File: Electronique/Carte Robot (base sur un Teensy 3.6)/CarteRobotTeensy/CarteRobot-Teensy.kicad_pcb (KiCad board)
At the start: 2 copper layers, 1 part, among them J1 Teensy-3.6

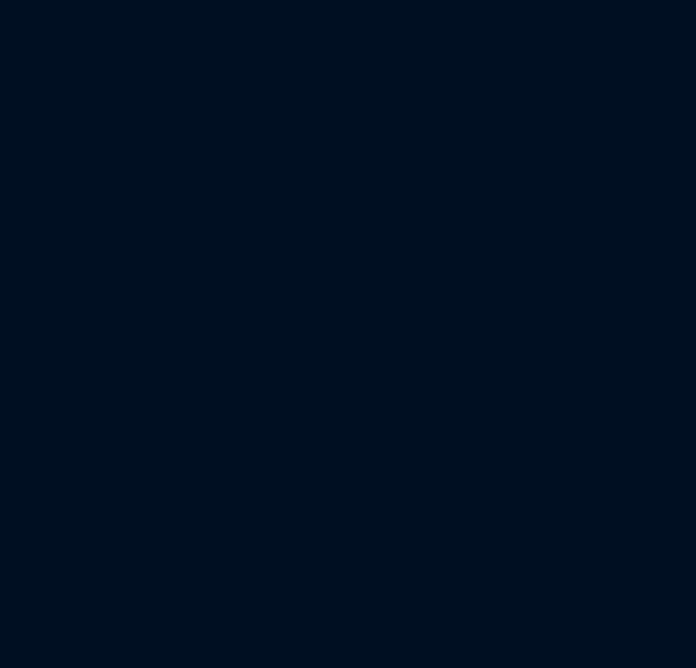
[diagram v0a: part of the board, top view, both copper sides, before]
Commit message: maj schema de la carte robot
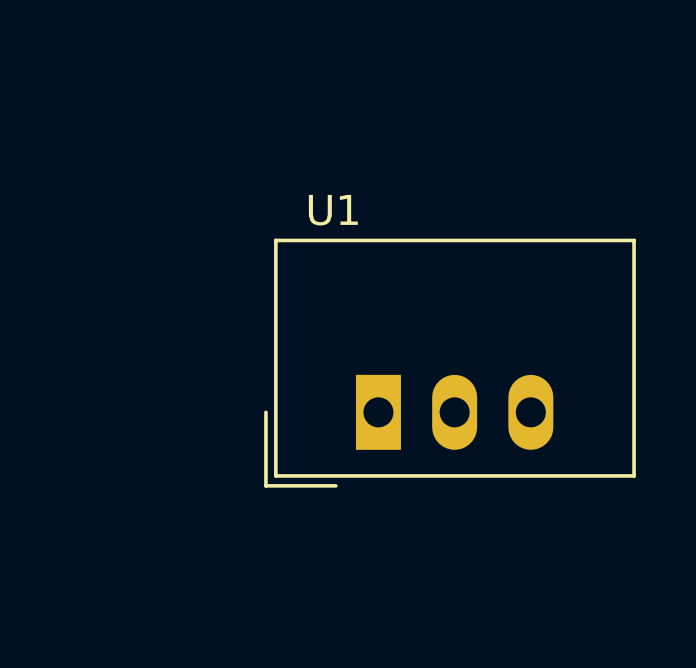
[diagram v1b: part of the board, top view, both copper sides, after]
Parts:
- added U1: TSR_1-2450, Converter_DCDC:Converter_DCDC_TRACO_TSR-1_THT, F.Cu at (397.5, 236.2)
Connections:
- J1 pad 1: Net-(J1-Pad1) -> GND
- J1 pad 34: Net-(J1-Pad34) -> GND
- J1 pad 48: Net-(J1-Pad48) -> +5V

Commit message: ajout driver schema de la carte
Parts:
- added A1: Pololu_Breakout_DRV8825, Module:Pololu_Breakout-16_15.2x20.3mm, F.Cu at (111.0, 102.0)
- added A2: Pololu_Breakout_DRV8825, Module:Pololu_Breakout-16_15.2x20.3mm, F.Cu at (134.7, 135.8)
- added D2: 1N4001, Diode_THT:D_DO-41_SOD81_P10.16mm_Horizontal, F.Cu at (130.0, 68.0)
- added J1: Conn_Bat2, Mes_empreintes:SL_3.50-02-180G_Weidmuller, F.Cu at (127.5, 58.0)
- added J10: Conn_01x03, Connector_PinHeader_2.54mm:PinHeader_1x03_P2.54mm_Vertical, F.Cu at (109.0, 123.0)
- added J11: Conn_AX12, Connector_Molex:Molex_SPOX_5267-03A_1x03_P2.50mm_Vertical, F.Cu at (218.0, 94.0)
- added J2: Conn_Bat1, Mes_empreintes:SL_3.50-02-180G_Weidmuller, F.Cu at (140.5, 58.0)
- added J3: Conn_OnOff, Connector_PinHeader_2.54mm:PinHeader_1x02_P2.54mm_Vertical, F.Cu at (117.0, 57.0)
- added J4: Conn_Aru, Connector_PinHeader_2.54mm:PinHeader_1x02_P2.54mm_Vertical, F.Cu at (104.0, 57.0)
- added J8: Conn_01x03, Connector_PinHeader_2.54mm:PinHeader_1x03_P2.54mm_Vertical, F.Cu at (92.0, 123.0)
- added J9: Conn_01x03, Connector_PinHeader_2.54mm:PinHeader_1x03_P2.54mm_Vertical, F.Cu at (101.0, 123.0)
- added U2: TSR_1-2465, Converter_DCDC:Converter_DCDC_TRACO_TSR-1_THT, F.Cu at (190.8, 38.3)
- added U3: TSR_1-2490, Converter_DCDC:Converter_DCDC_TRACO_TSR-1_THT, F.Cu at (190.8, 53.0)
- moved U1 334.2 mm to (107.0, 71.0)
- moved J5 322.4 mm to (61.9, 74.5)
- renumbered J1 to J5
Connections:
- net Net-(J1-Pad45) renamed /Vbat
- J5 pad 15: Net-(J1-Pad15) -> +3V3
- J5 pad 27: Net-(J1-Pad27) -> /STEP_D
- J5 pad 28: Net-(J1-Pad28) -> /STEP_G
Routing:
- net /M2: track 0.00 -> 16.8 mm
- net /M0: track 0.00 -> 14.4 mm
- net /M1: track 0.00 -> 13.4 mm
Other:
- board outline added: 100 x 100 mm

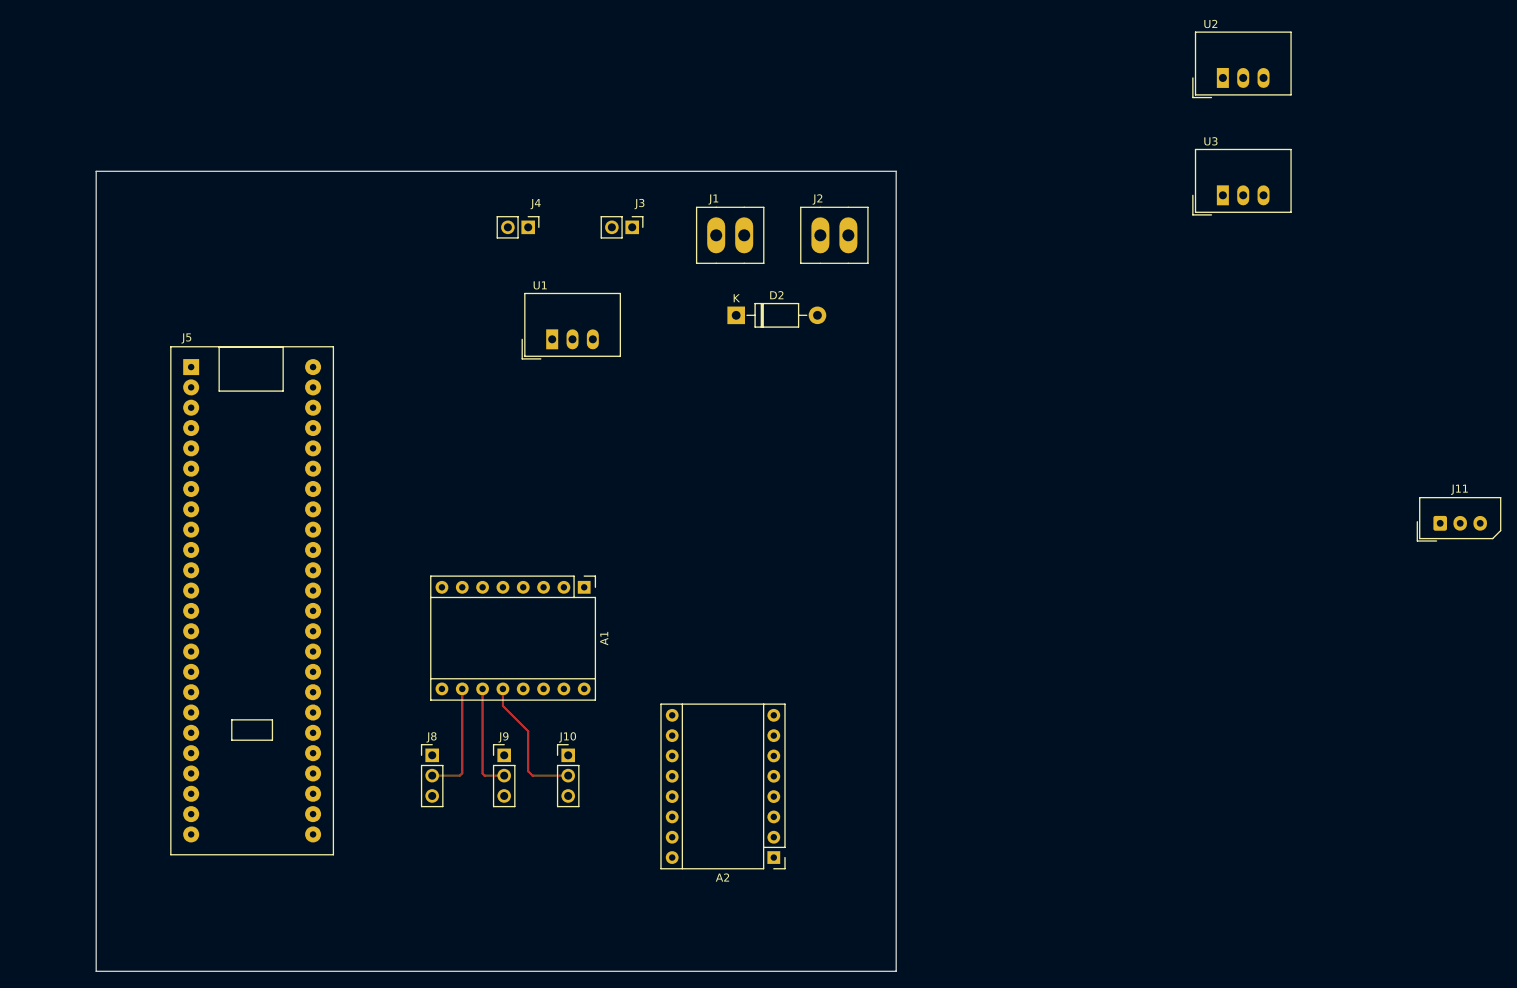
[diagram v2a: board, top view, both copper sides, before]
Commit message: ajouts des connecteurs pour l'uart
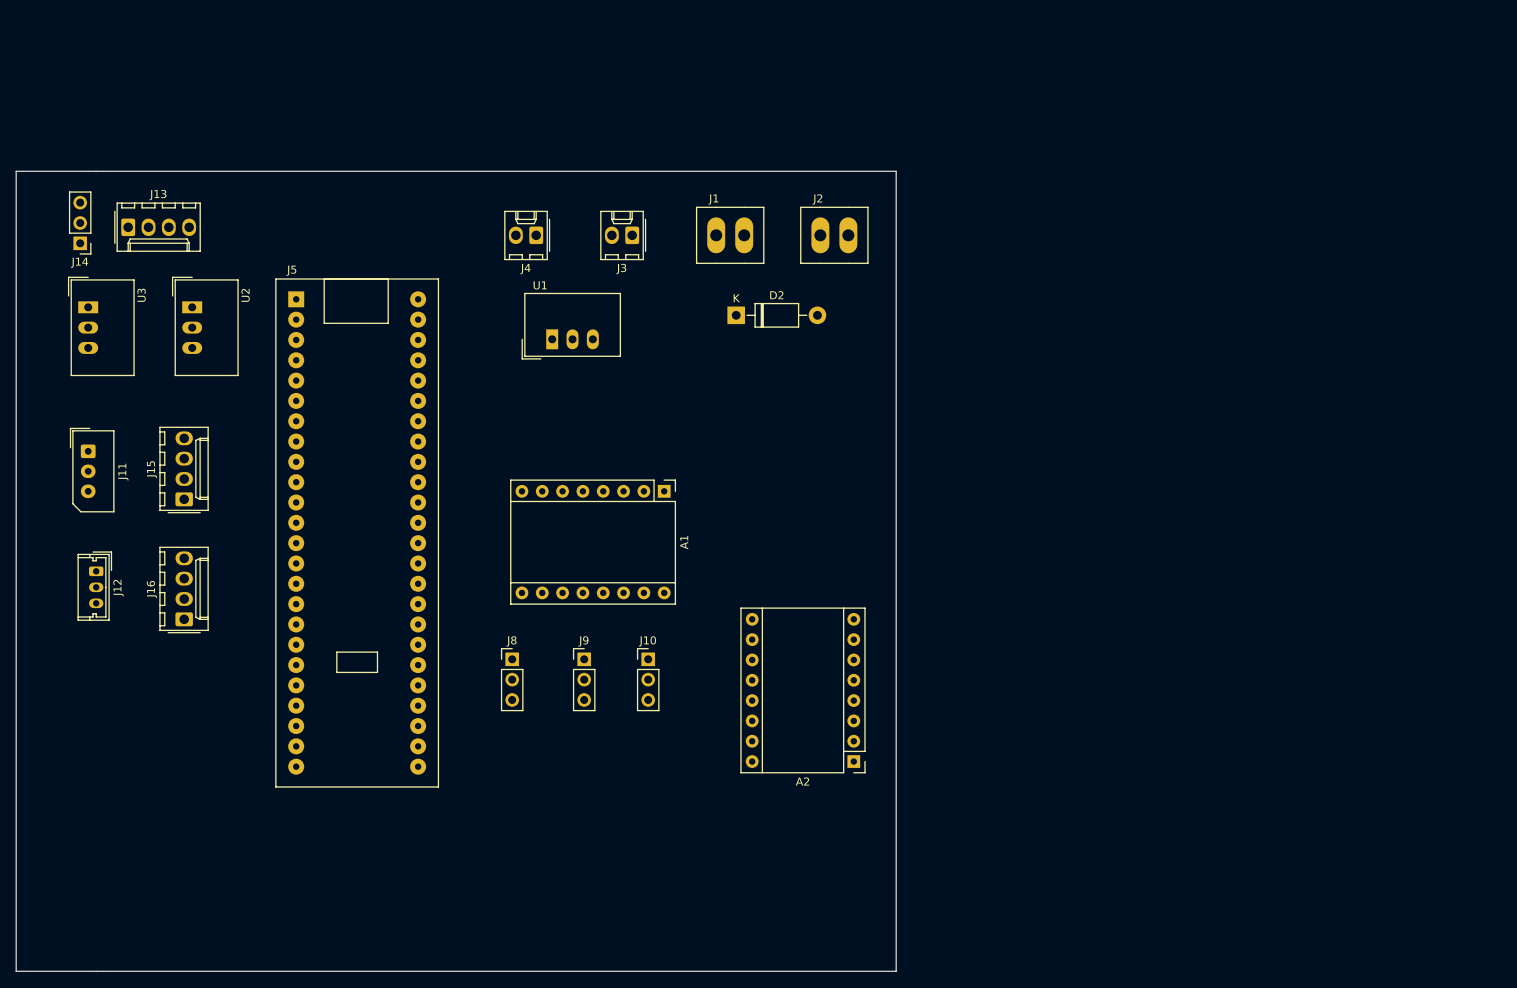
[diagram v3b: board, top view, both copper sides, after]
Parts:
- added J12: Conn_XL320, Connector_Molex:Molex_Micro-Latch_53253-0370_1x03_P2.00mm_Vertical, F.Cu at (50.0, 100.0)
- added J13: Conn_01x04, Connector_Molex:Molex_KK-254_AE-6410-04A_1x04_P2.54mm_Vertical, F.Cu at (54.0, 57.0)
- added J14: Conn_01x03, Connector_PinHeader_2.54mm:PinHeader_1x03_P2.54mm_Vertical, F.Cu at (48.0, 59.0)
- added J15: Conn_01x04, Connector_Molex:Molex_KK-254_AE-6410-04A_1x04_P2.54mm_Vertical, F.Cu at (61.0, 91.0)
- added J16: Conn_01x04, Connector_Molex:Molex_KK-254_AE-6410-04A_1x04_P2.54mm_Vertical, F.Cu at (61.0, 106.0)
- J3, J4: footprint Connector_PinHeader_2.54mm:PinHeader_1x02_P2.54mm_Vertical -> Connector_Molex:Molex_KK-254_AE-6410-02A_1x02_P2.54mm_Vertical
- moved J11 169.2 mm to (49.0, 85.0), turned to 270 degrees
- moved U3 142.5 mm to (49.0, 67.0), turned to 270 degrees
- moved U2 132.0 mm to (62.0, 67.0), turned to 270 degrees
- moved J5 15.6 mm to (75.0, 66.0)
- moved A1 15.6 mm to (121.0, 90.0)
- moved A2 15.6 mm to (144.7, 123.8)
- moved J10 15.6 mm to (119.0, 111.0)
- moved J8 15.6 mm to (102.0, 111.0)
- moved J9 15.6 mm to (111.0, 111.0)
- moved J4 1.41 mm to (105.0, 58.0), turned to 180 degrees
- moved J3 1.00 mm to (117.0, 58.0), turned to 180 degrees
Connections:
- net Net-(J5-Pad2) renamed /RX1
- net Net-(J5-Pad3) renamed /TX1
- J11 pad 1: Net-(J11-Pad1) -> GND
- J11 pad 2: Net-(J11-Pad2) -> +9V
- J11 pad 3: Net-(J11-Pad3) -> /TX3
- J5 pad 10: Net-(J5-Pad10) -> /TX2
- J5 pad 7: Net-(J5-Pad7) -> /RX3
- J5 pad 8: Net-(J5-Pad8) -> /TX3
- J5 pad 9: Net-(J5-Pad9) -> /RX2
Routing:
- net /M2: track 16.8 -> 0.00 mm
- net /M0: track 14.4 -> 0.00 mm
- net /M1: track 13.4 -> 0.00 mm
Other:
- board size 100 x 100 mm -> 110 x 100 mm

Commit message: ajouts connecteurs, leds
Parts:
- added C1: 100u, Capacitor_THT:CP_Radial_D6.3mm_P2.50mm, F.Cu at (103.0, 92.0)
- added C2: 100u, Capacitor_THT:CP_Radial_D6.3mm_P2.50mm, F.Cu at (132.0, 110.0)
- added D1: LED, LED_THT:LED_D5.0mm_Clear, F.Cu at (122.0, 68.0)
- added J17: Conn_01x04, Connector_Molex:Molex_KK-254_AE-6410-04A_1x04_P2.54mm_Vertical, F.Cu at (70.5, 133.0)
- added J18: Conn_01x04, Connector_Molex:Molex_KK-254_AE-6410-04A_1x04_P2.54mm_Vertical, F.Cu at (86.0, 133.0)
- added J19: Conn_01x03, Connector_Molex:Molex_KK-254_AE-6410-03A_1x03_P2.54mm_Vertical, F.Cu at (144.0, 71.0)
- added J20: Conn_01x04, Connector_Molex:Molex_KK-254_AE-6410-04A_1x04_P2.54mm_Vertical, F.Cu at (144.0, 81.5)
- added J21: Conn_01x04, Connector_Molex:Molex_KK-254_AE-6410-04A_1x04_P2.54mm_Vertical, F.Cu at (135.0, 81.5)
- added J6: Conn_01x04, Connector_Molex:Molex_KK-254_AE-6410-04A_1x04_P2.54mm_Vertical, F.Cu at (145.0, 96.5)
- added J7: Conn_01x04, Connector_Molex:Molex_KK-254_AE-6410-04A_1x04_P2.54mm_Vertical, F.Cu at (145.0, 117.0)
- added R1: 100k, Resistor_SMD:R_0805_2012Metric_Pad1.20x1.40mm_HandSolder, F.Cu at (116.0, 66.0)
- moved J10 14.0 mm to (119.0, 125.0), turned to 180 degrees
- moved J8 14.0 mm to (102.0, 125.0), turned to 180 degrees
- moved J9 14.0 mm to (111.0, 125.0), turned to 180 degrees
- moved A2 11.7 mm to (139.0, 134.0)
- moved A1 9.00 mm to (121.0, 99.0)
- moved U1 6.32 mm to (109.0, 65.0), turned to 180 degrees
- moved D2 3.61 mm to (128.0, 65.0)
- moved J13 3.00 mm to (57.0, 57.0)
- moved J14 3.00 mm to (51.0, 59.0)
- moved J1 2.83 mm to (125.5, 56.0)
- moved J3 2.52 mm to (115.5, 56.0), turned to 0 degrees
- moved J2 2.51 mm to (139.0, 56.0)
- moved J4 2.24 mm to (104.0, 56.0), turned to 0 degrees
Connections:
- A1 pad 2: Net-(A1-Pad2) -> (no net)
- A1 pad 4: Net-(A1-Pad4) -> /A1D
- A1 pad 9: /EN_D -> /EN
- A2 pad 2: Net-(A2-Pad2) -> (no net)
- A2 pad 4: Net-(A2-Pad4) -> /A1G
- A2 pad 9: /EN_G -> /EN
- J13 pad 3: Net-(J13-Pad3) -> (no net)
- J13 pad 4: Net-(J13-Pad4) -> (no net)
- J3 pad 1: Net-(D2-Pad1) -> /Von
- J3 pad 2: /Von -> Net-(D2-Pad1)
- J4 pad 1: /Von -> /Varu
- J4 pad 2: /Varu -> /Von
- J5 pad 11: Net-(J5-Pad11) -> (no net)
- J5 pad 12: Net-(J5-Pad12) -> (no net)
- J5 pad 13: Net-(J5-Pad13) -> (no net)
- J5 pad 14: Net-(J5-Pad14) -> (no net)
- J5 pad 16: Net-(J5-Pad16) -> (no net)
- J5 pad 17: Net-(J5-Pad17) -> (no net)
- J5 pad 18: Net-(J5-Pad18) -> (no net)
- J5 pad 19: Net-(J5-Pad19) -> (no net)
- J5 pad 2: /RX1 -> (no net)
- J5 pad 20: Net-(J5-Pad20) -> (no net)
- J5 pad 21: Net-(J5-Pad21) -> (no net)
- J5 pad 22: Net-(J5-Pad22) -> (no net)
- J5 pad 23: Net-(J5-Pad23) -> /RX4
- J5 pad 24: Net-(J5-Pad24) -> /TX4
- J5 pad 25: Net-(J5-Pad25) -> /TX5
- J5 pad 26: Net-(J5-Pad26) -> /RX5
- J5 pad 27: /STEP_D -> /STEP_G
- J5 pad 28: /STEP_G -> /DIR_G
- J5 pad 29: Net-(J5-Pad29) -> /EN
- J5 pad 3: /TX1 -> (no net)
- J5 pad 30: Net-(J5-Pad30) -> /STEP_D
- J5 pad 31: Net-(J5-Pad31) -> /DIR_D
- J5 pad 32: Net-(J5-Pad32) -> (no net)
- J5 pad 33: Net-(J5-Pad33) -> (no net)
- J5 pad 35: Net-(J5-Pad35) -> (no net)
- J5 pad 36: Net-(J5-Pad36) -> (no net)
- J5 pad 37: Net-(J5-Pad37) -> (no net)
- J5 pad 38: Net-(J5-Pad38) -> (no net)
- J5 pad 39: Net-(J5-Pad39) -> (no net)
- J5 pad 4: Net-(J5-Pad4) -> (no net)
- J5 pad 40: Net-(J5-Pad40) -> /SDA0
- J5 pad 41: Net-(J5-Pad41) -> /SCL0
- J5 pad 42: Net-(J5-Pad42) -> /20
- J5 pad 43: Net-(J5-Pad43) -> /21
- J5 pad 44: Net-(J5-Pad44) -> /22
- J5 pad 45: /Vbat -> (no net)
- J5 pad 46: Net-(J5-Pad46) -> (no net)
- J5 pad 47: Net-(J5-Pad47) -> (no net)
- J5 pad 5: Net-(J5-Pad5) -> (no net)
- J5 pad 6: Net-(J5-Pad6) -> (no net)
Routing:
- net /22: track 0.00 -> 55.9 mm
- net /21: track 0.00 -> 55.9 mm
- net /20: track 0.00 -> 55.9 mm
- net /SCL0: track 0.00 -> 54.7 mm
- net /SDA0: track 0.00 -> 54.7 mm
- net /Varu: track 0.00 -> 49.2 mm
- net /DIR_D: track 0.00 -> 34.6 mm
- net /STEP_D: track 0.00 -> 31.2 mm
- net +5V: track 0.00 -> 27.5 mm
- net /Von: track 0.00 -> 18.9 mm
- net Net-(D2-Pad1): track 0.00 -> 17.5 mm
- net /M2: track 0.00 -> 15.0 mm
- net /EN: track 0.00 -> 14.7 mm
- net /M0: track 0.00 -> 12.3 mm
- net /M1: track 0.00 -> 11.9 mm
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
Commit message: adaptateur servo Dynamixel + connecteur SPI
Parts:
- removed J16, J17, J20, J21: Conn_01x04, Connector_Molex:Molex_KK-254_AE-6410-04A_1x04_P2.54mm_Vertical
- removed J19: Conn_01x03, Connector_Molex:Molex_KK-254_AE-6410-03A_1x03_P2.54mm_Vertical
- removed U2: TSR_1-2465, Converter_DCDC:Converter_DCDC_TRACO_TSR-1_THT
- removed U3: TSR_1-2490, Converter_DCDC:Converter_DCDC_TRACO_TSR-1_THT
- added J22: Conn_01x07, Connector_Molex:Molex_KK-254_AE-6410-07A_1x07_P2.54mm_Vertical, F.Cu at (144.3, 70.7)
- J11: value Conn_AX12 -> Conn_01x05; footprint Connector_Molex:Molex_SPOX_5267-03A_1x03_P2.50mm_Vertical -> Connector_Molex:Molex_KK-254_AE-6410-05A_1x05_P2.54mm_Vertical
- J12: value Conn_XL320 -> Conn_01x05; footprint Connector_Molex:Molex_Micro-Latch_53253-0370_1x03_P2.00mm_Vertical -> Connector_Molex:Molex_KK-254_AE-6410-05A_1x05_P2.54mm_Vertical
- J14: value Conn_01x03 -> Conn_02x04_Counter_Clockwise; footprint Connector_PinHeader_2.54mm:PinHeader_1x03_P2.54mm_Vertical -> Connector_PinHeader_2.54mm:PinHeader_2x04_P2.54mm_Vertical
- J18: value Conn_01x04 -> Adaptateur-Servo-Dynamixel; footprint Connector_Molex:Molex_KK-254_AE-6410-04A_1x04_P2.54mm_Vertical -> Mes_empreintes:Adaptateur-Servo-Dynamixel
- R1: footprint Resistor_SMD:R_0805_2012Metric_Pad1.20x1.40mm_HandSolder -> Resistor_THT:R_Axial_DIN0207_L6.3mm_D2.5mm_P10.16mm_Horizontal
- moved J18 71.8 mm to (58.6, 66.7)
- moved J11 64.5 mm to (92.5, 132.7), turned to 180 degrees
- moved J14 45.2 mm to (58.8, 103.5), turned to 90 degrees
- moved J12 42.2 mm to (76.6, 132.7), turned to 180 degrees
- moved J13 8.74 mm to (65.7, 56.2)
- moved R1 5.14 mm to (115.6, 71.1)
- moved J15 3.05 mm to (63.7, 89.6)
- moved J2 1.78 mm to (137.2, 56.0)
- moved U1 1.28 mm to (107.7, 64.7)
- moved J6 0.71 mm to (144.3, 96.4)
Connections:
- J11 pad 1: GND -> +5V
- J11 pad 2: +9V -> GND
- J11 pad 3: /TX3 -> (no net)
- J12 pad 1: GND -> +5V
- J12 pad 2: /6.5V -> GND
- J12 pad 3: /TX2 -> (no net)
- J13 pad 1: Net-(J13-Pad1) -> /Varu
- J13 pad 2: GND -> /RX2
- J13 pad 3: (no net) -> /TX2
- J13 pad 4: (no net) -> GND
- J14 pad 1: +9V -> /IRQ
- J14 pad 2: Net-(J13-Pad1) -> /MISO1
- J14 pad 3: /6.5V -> /MOSI1
- J18 pad 1: +5V -> /Varu
- J18 pad 2: GND -> /TX3
- J18 pad 3: /TX5 -> /RX3
- J18 pad 4: /RX5 -> (no net)
- J5 pad 10: /TX2 -> /TX3
- J5 pad 11: (no net) -> /RX2
- J5 pad 12: (no net) -> /TX2
- J5 pad 14: (no net) -> /CE
- J5 pad 16: (no net) -> /IRQ
- J5 pad 2: (no net) -> /MOSI1
- J5 pad 23: /RX4 -> /CS1
- J5 pad 24: /TX4 -> /SCK1
- J5 pad 25: /TX5 -> (no net)
- J5 pad 26: /RX5 -> (no net)
- J5 pad 3: (no net) -> /MISO1
- J5 pad 7: /RX3 -> (no net)
- J5 pad 8: /TX3 -> (no net)
- J5 pad 9: /RX2 -> /RX3
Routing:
- net /Varu: track 49.2 -> 86.7 mm
- net /CS1: track 0.00 -> 25.7 mm
- net /CE: track 0.00 -> 12.5 mm
- net GND: track 10.8 -> 0.00 mm
- net Net-(J1-Pad2): track 10.0 -> 0.00 mm
- net +3V3: track 0.00 -> 9.44 mm
- net Net-(D1-Pad2): track 6.19 -> 9.40 mm
- net +5V: track 27.5 -> 29.5 mm
- net /SDA0: track 54.7 -> 56.5 mm
- net /SCL0: track 54.7 -> 56.4 mm
- net /21: track 55.9 -> 57.0 mm
- net /Von: track 18.9 -> 18.2 mm
